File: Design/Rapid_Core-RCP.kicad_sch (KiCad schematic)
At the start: 34 parts, among them IC1 SHT30A-DIS-B2.5KS, J7 SWD_Debug, J8 GPIO_CONN_x_4, U1 STM32F446RETx, U3 CRE1S0505S3C, U6 CRE1S0505S3C, Y1 8_MHz, Y2 32.768_KHz

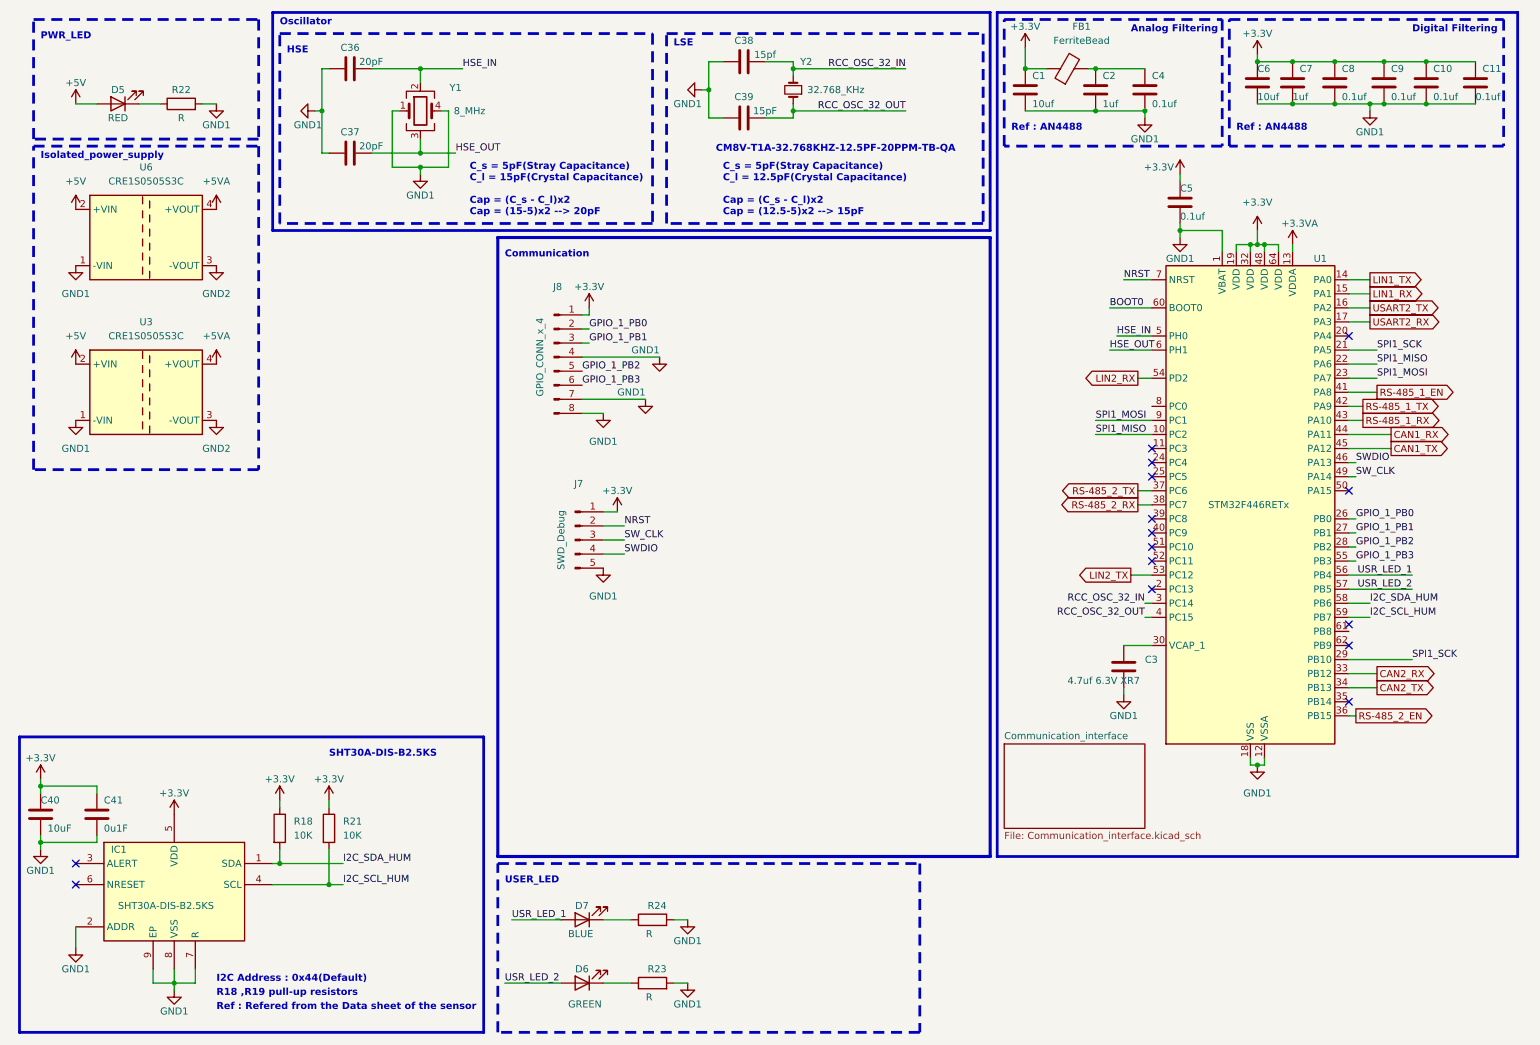
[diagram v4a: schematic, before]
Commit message: LIN,I2C,SPI,SWD added , Power_stage created
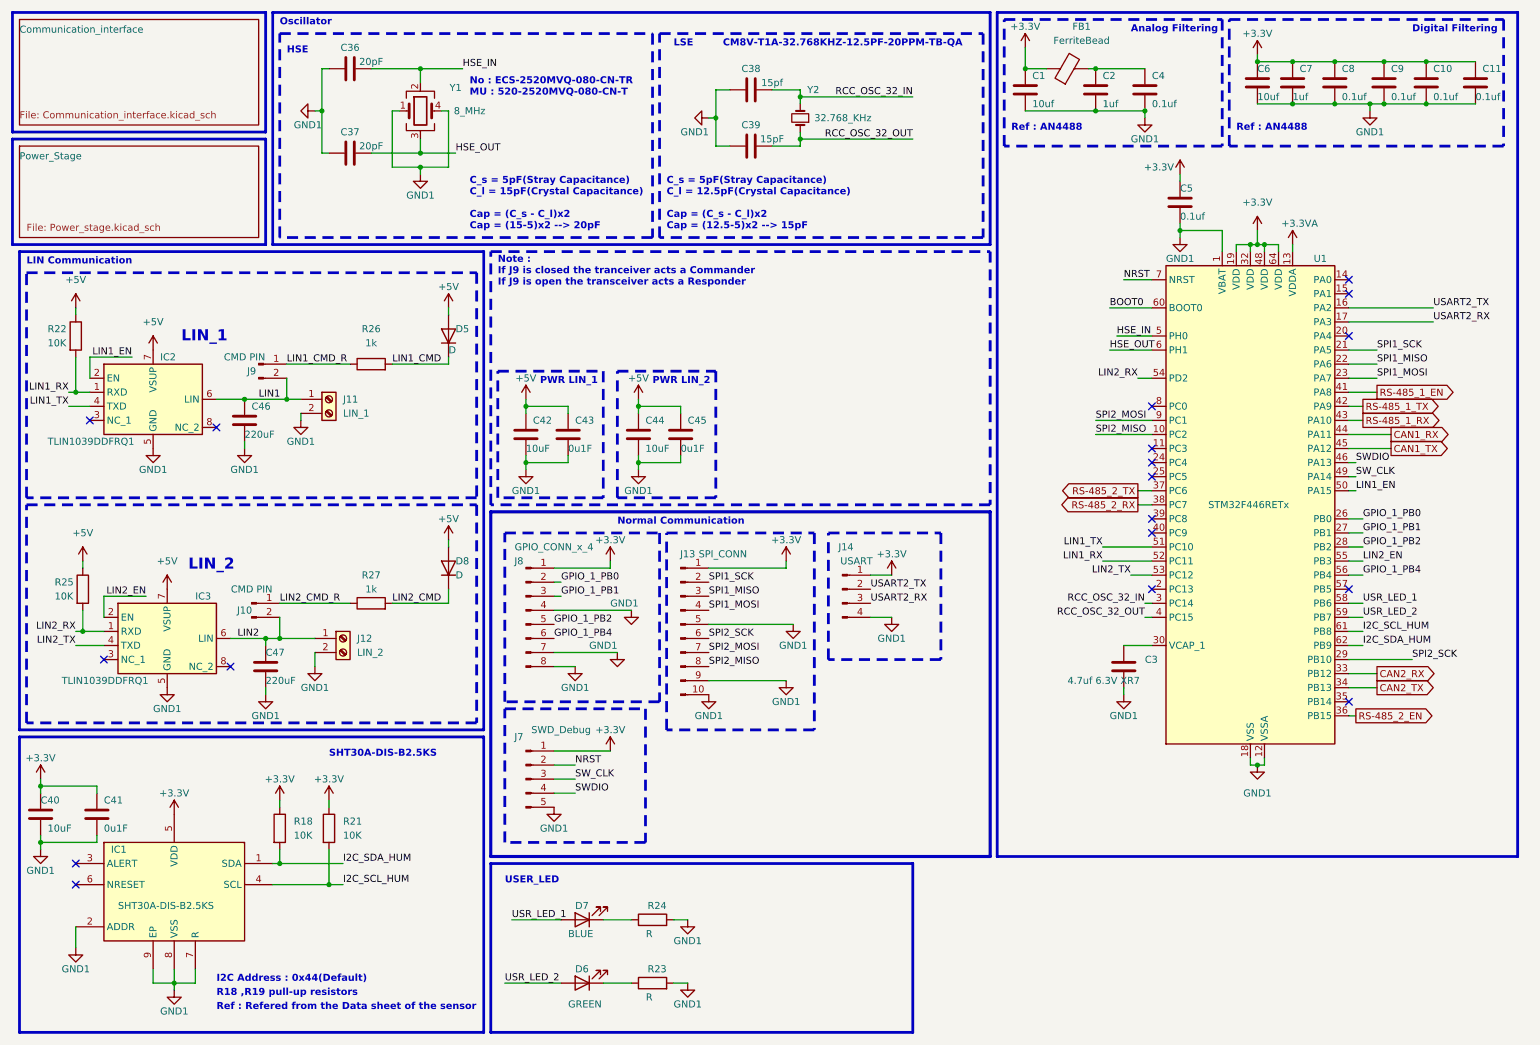
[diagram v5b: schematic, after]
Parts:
- removed D5: RED, symbol Device:LED
- removed U3, U6: CRE1S0505S3C, Converter_DCDC:Converter_DCDC_Murata_CRE1xxxxxx3C_THT, symbol Regulator_Switching:CRE1S0505S3C
- added C42, C44: 10uF, symbol Device:C
- added C43, C45: 0u1F, symbol Device:C
- added C46, C47: 220uF, symbol Device:C
- added D5, D8: D, symbol Device:D
- added IC2, IC3: TLIN1039DDFRQ1, TLIN1039DDFRQ1:SOT65P280X110-8N, symbol TLIN1039DDFRQ1:TLIN1039DDFRQ1
- added J10, J9: CMD PIN, symbol Connector:Conn_01x02_Pin
- added J11: LIN_1, symbol Connector:Screw_Terminal_01x02
- added J12: LIN_2, symbol Connector:Screw_Terminal_01x02
- added J13: SPI_CONN, symbol Connector:Conn_01x10_Pin
- added J14: USART, symbol Connector:Conn_01x04_Pin
- added R25: 10K, symbol Device:R
- added R26, R27: 1k, symbol Device:R
- R22: value R -> 10K
- Y1: footprint Crystal:Crystal_SMD_Abracon_ABM10-4Pin_2.5x2.0mm -> ECS-2520MVLC_8MHz:ECS2520MVLC080BNTR
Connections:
- net +3.3V: now also J13.1 (Pin_1), J14.1 (Pin_1)
- net +5V: now also R22.1, C42.1, C43.1, C44.1, C45.1, D5.2 (A), D8.2 (A), IC2.7 (VSUP), IC3.7 (VSUP), R25.1
- net GND1: now also C42.2, C43.2, C44.2, C45.2, C46.2, C47.2, IC2.5 (GND), IC3.5 (GND), J11.2 (Pin_2), J12.2 (Pin_2), J13.10 (Pin_10), J13.5 (Pin_5), J13.9 (Pin_9), J14.4 (Pin_4); no longer R22.2
- net I2C_SCL_HUM: now also U1.61 (PB8); no longer U1.59 (PB7)
- net I2C_SDA_HUM: now also U1.62 (PB9); no longer U1.58 (PB6)
- net LIN1_RX: now also R22.2, U1.52 (PC11), IC2.1 (RXD); no longer U1.15 (PA1)
- net LIN1_TX: now also U1.51 (PC10), IC2.4 (TXD); no longer U1.14 (PA0)
- net LIN2_RX: now also IC3.1 (RXD), R25.2
- net LIN2_TX: now also IC3.4 (TXD)
- net SPI1_MISO: now also J13.3 (Pin_3); no longer U1.10 (PC2)
- net SPI1_MOSI: now also J13.4 (Pin_4); no longer U1.9 (PC1)
- net SPI1_SCK: now also J13.2 (Pin_2); no longer U1.29 (PB10)
- net USART2_RX: now also J14.3 (Pin_3)
- net USART2_TX: now also J14.2 (Pin_2)
- net USR_LED_1: now also U1.58 (PB6); no longer U1.56 (PB4)
- net USR_LED_2: now also U1.59 (PB7); no longer U1.57 (PB5)
- net LIN1_EN: now reaches U1.50 (PA15)
- net LIN1_EN: now also IC2.2 (EN)
- net GPIO_1_PB3 renamed GPIO_1_PB4
- net GPIO_1_PB4: now also U1.56 (PB4); no longer U1.55 (PB3)
- new net LIN1: C46.1, IC2.6 (LIN), J11.1 (Pin_1), J9.2 (Pin_2)
- new net LIN1_CMD: D5.1 (K), R26.2
- new net LIN1_CMD_R: J9.1 (Pin_1), R26.1
- new net LIN2: C47.1, IC3.6 (LIN), J10.2 (Pin_2), J12.1 (Pin_1)
- new net LIN2_CMD: D8.1 (K), R27.2
- new net LIN2_CMD_R: J10.1 (Pin_1), R27.1
- new net LIN2_EN: IC3.2 (EN), U1.55 (PB3)
- new net SPI2_MISO: J13.8 (Pin_8), U1.10 (PC2)
- new net SPI2_MOSI: J13.7 (Pin_7), U1.9 (PC1)
- new net SPI2_SCK: J13.6 (Pin_6), U1.29 (PB10)
- no-connect marks 15 -> 18
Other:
- added sheet Power_Stage (Power_stage.kicad_sch)
- note added: "LIN Communication"
- note added: "LIN_1"
- note added: "LIN_2"
- note added: "No : ECS-2520MVQ-080-CN-TR MU : 520-2520MVQ-080-CN-T"
- note added: "Normal Communication"
- note added: "Note : If J9 is closed the tranceiver acts a Commander If J9 is open the transceiver acts a Responder"
- note added: "PWR LIN_1"
- note added: "PWR LIN_2"
- note removed: "Communication"
- note removed: "Isolated_power_supply"
- note removed: "PWR_LED"
- moved on the sheet: C38, C39, J7, J8, Y2

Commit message: Setup Power supply
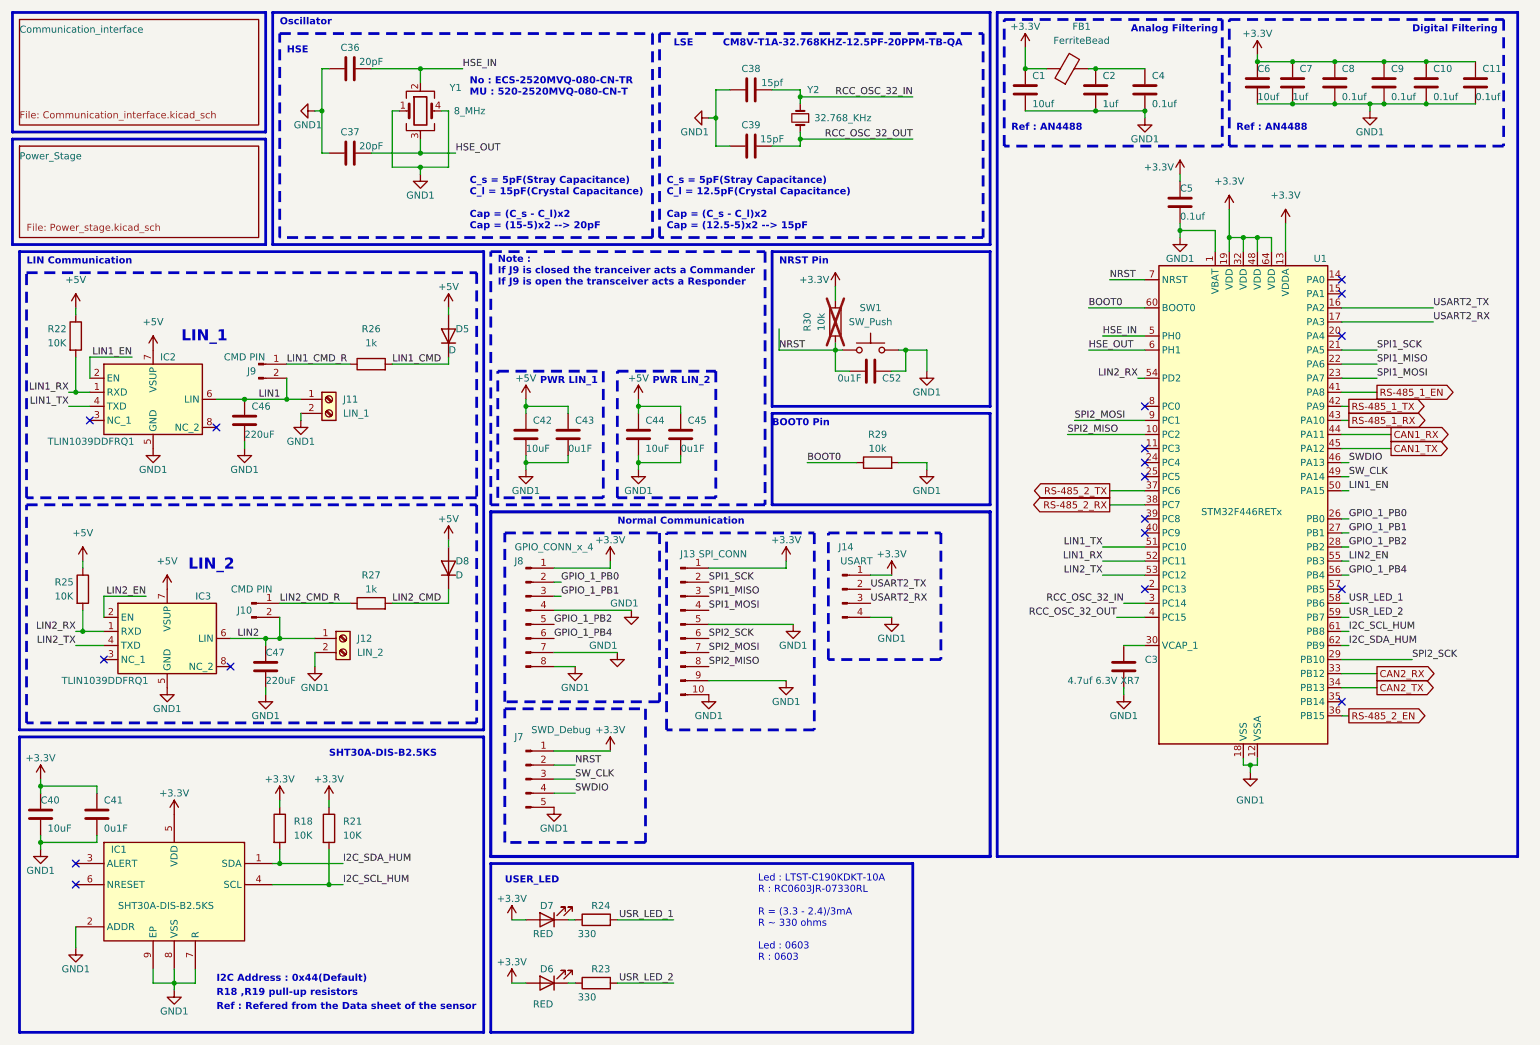
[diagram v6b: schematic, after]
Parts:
- added C52: 0u1F, symbol Device:C
- added R29, R30: 10k, symbol Device:R
- added SW1: SW_Push, symbol Switch:SW_Push
- D6: value GREEN -> RED
- D7: value BLUE -> RED
- R23, R24: value R -> 330
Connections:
- net +3.3VA is gone; now on net +3.3V: U1.13 (VDDA)
- net +3.3V: now also D6.2 (A), D7.2 (A), R30.2
- net BOOT0: now also R29.1
- net GND1: now also C52.2, R29.2, SW1.2; no longer R23.2, R24.2
- net NRST: now also C52.1, R30.1, SW1.1
- net USR_LED_1: now also R24.2; no longer D7.2 (A)
- net USR_LED_2: now also R23.2; no longer D6.2 (A)
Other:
- note added: "BOOT0 Pin"
- note added: "Led : LTST-C190KDKT-10A R : RC0603JR-07330RL R = (3.3 - 2.4)/3mA R ~ 330 ohms Led : 0603 R : 0603"
- note added: "NRST Pin"
- moved on the sheet: D6, D7, R23, R24

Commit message: Footprints added to all componenets
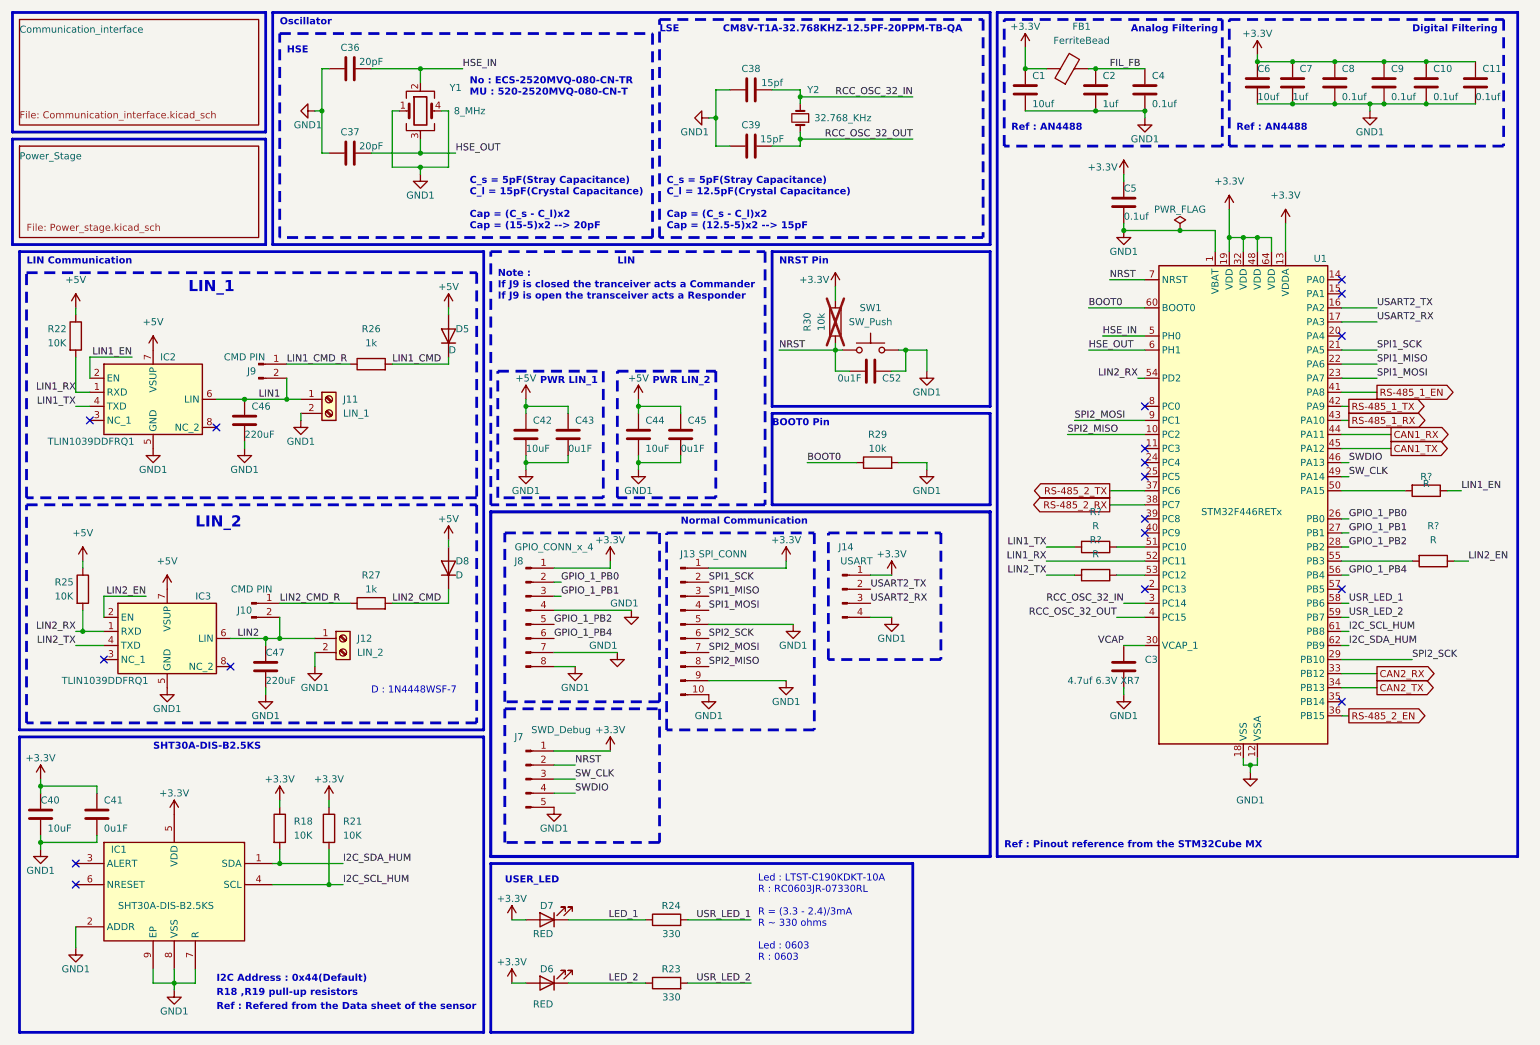
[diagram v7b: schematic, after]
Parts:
- added R? (x4): R, symbol Device:R
- C1, C40, C42, C44, C46, C47, C6: footprint (none) -> Capacitor_SMD:C_0805_2012Metric_Pad1.18x1.45mm_HandSolder
- C10, C11, C2, C4, C41, C43, C45, C5, C52, C7, C8, C9: footprint (none) -> Capacitor_SMD:C_0603_1608Metric_Pad1.08x0.95mm_HandSolder
- C36, C37, C38, C39: footprint (none) -> Capacitor_SMD:C_0603_1608Metric
- D5, D8: footprint (none) -> Diode_SMD:D_SOD-323_HandSoldering
- D6, D7: footprint (none) -> LED_SMD:LED_0603_1608Metric_Pad1.05x0.95mm_HandSolder
- J13: footprint (none) -> Connector_PinHeader_2.54mm:PinHeader_1x10_P2.54mm_Vertical
- J14: footprint (none) -> Connector_PinHeader_2.54mm:PinHeader_1x04_P2.54mm_Vertical
- J7: footprint (none) -> Connector_PinHeader_2.54mm:PinHeader_1x05_P2.54mm_Vertical
- J8: footprint (none) -> Connector_PinHeader_2.54mm:PinHeader_1x08_P2.54mm_Vertical
- J9: footprint (none) -> Connector_PinHeader_2.54mm:PinHeader_1x02_P2.54mm_Vertical
- R18, R21, R22, R25, R26, R27, R29, R30: footprint (none) -> Resistor_SMD:R_0805_2012Metric_Pad1.20x1.40mm_HandSolder
- R23, R24: footprint (none) -> Resistor_SMD:R_0603_1608Metric_Pad0.98x0.95mm_HandSolder
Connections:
- net LIN1_EN: now also R?.1; no longer U1.50 (PA15)
- net LIN1_TX: now also R?.2; no longer U1.51 (PC10)
- net LIN2_EN: now also R?.1; no longer U1.55 (PB3)
- net LIN2_TX: now also R?.2; no longer U1.53 (PC12)
- net LED_1: now reaches D7.1 (K), R24.1
- net FIL_FB: now reaches C2.1, C4.1, FB1.2
- net LED_2: now reaches D6.1 (K), R23.1
- net VCAP: now reaches C3.1, U1.30 (VCAP_1)
- new net: R?.2, U1.50 (PA15)
- new net: R?.2, U1.55 (PB3)
- new net: R?.1, U1.51 (PC10)
- new net: R?.1, U1.53 (PC12)
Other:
- note added: "D : 1N4448WSF-7"
- note added: "LIN"
- note added: "Ref : Pinout reference from the STM32Cube MX"
- moved on the sheet: C5, R23, R24

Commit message: CMC component name added
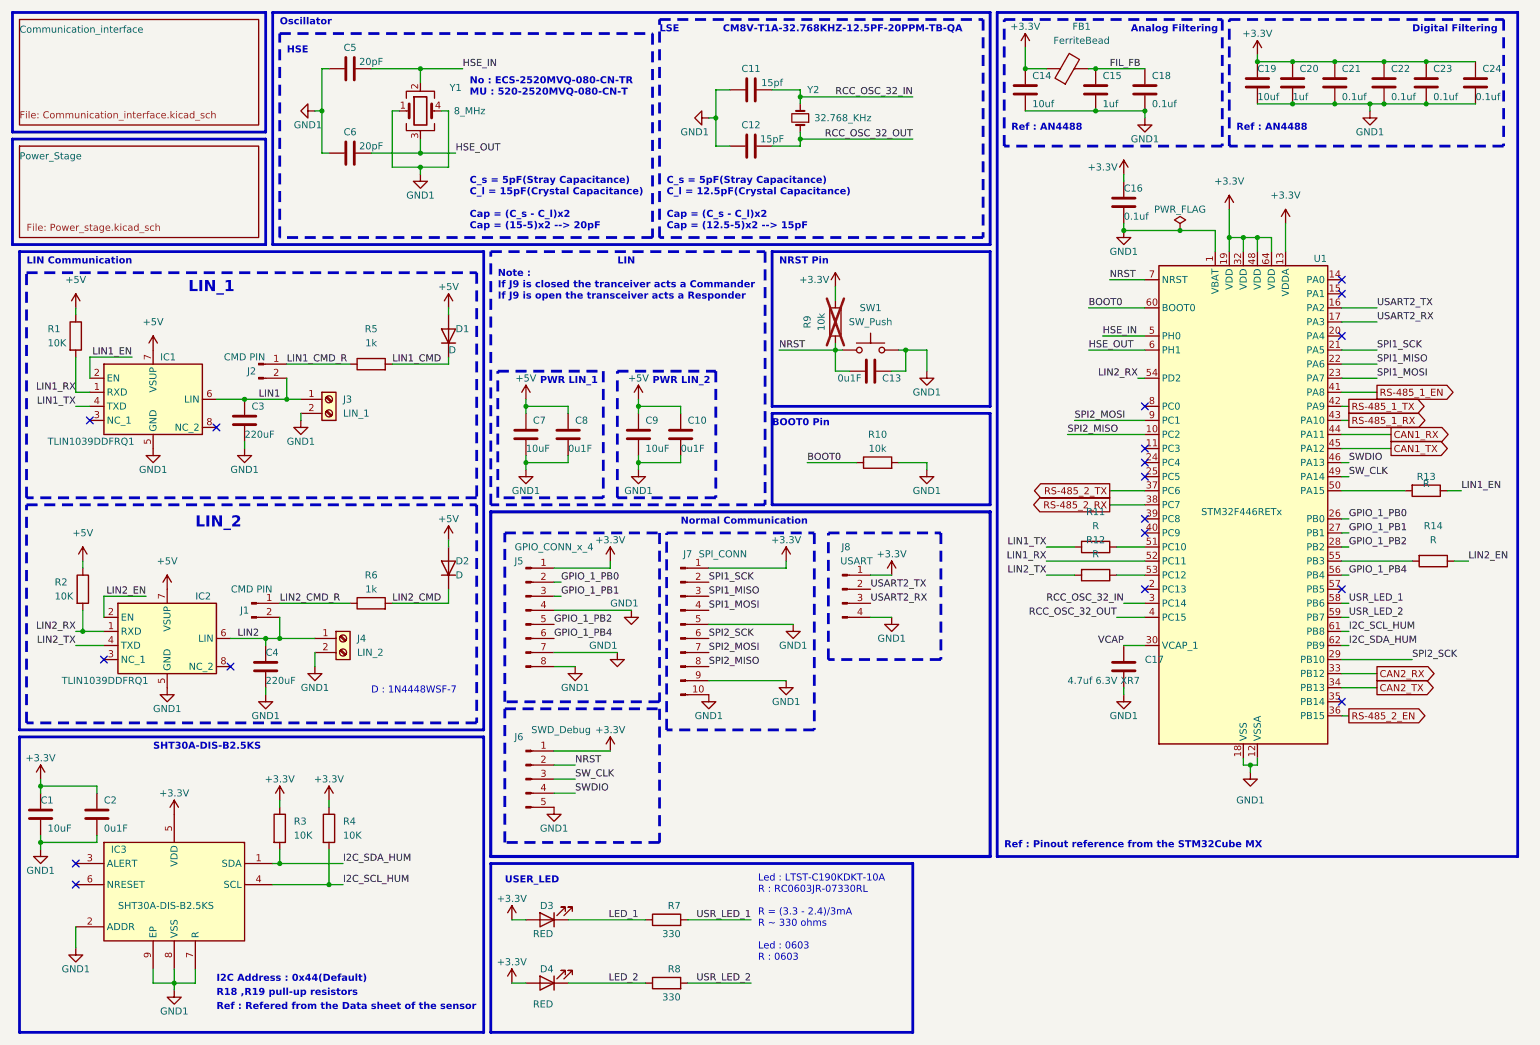
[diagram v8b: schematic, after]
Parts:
- gave numbers to parts that had none: 4
- renumbered C40 to C1, C45 to C10, C38 to C11, C39 to C12, C52 to C13, C1 to C14, C2 to C15, C5 to C16, C3 to C17, C4 to C18, C6 to C19, C41 to C2, C7 to C20, C8 to C21, C9 to C22, C10 to C23, C11 to C24, C46 to C3, C47 to C4, C36 to C5, C37 to C6, C42 to C7, C43 to C8, C44 to C9, D5 to D1, D8 to D2, D7 to D3, D6 to D4, IC2 to IC1, IC3 to IC2, IC1 to IC3, J10 to J1, J9 to J2, J11 to J3, J12 to J4, J8 to J5, J7 to J6, J13 to J7, J14 to J8, R22 to R1, R29 to R10, R25 to R2, R18 to R3, R21 to R4, R26 to R5, R27 to R6, R24 to R7, R23 to R8, R30 to R9
